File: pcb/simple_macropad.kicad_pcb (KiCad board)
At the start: 2 copper layers, 96 x 88 mm, 34 parts, among them J3 OLED_128x32, SW1 RotaryEncoder_Switch, SW2 RotaryEncoder_Switch, U2 PCF8574A, U3 MCU_Seeed_XIAO_RP2040

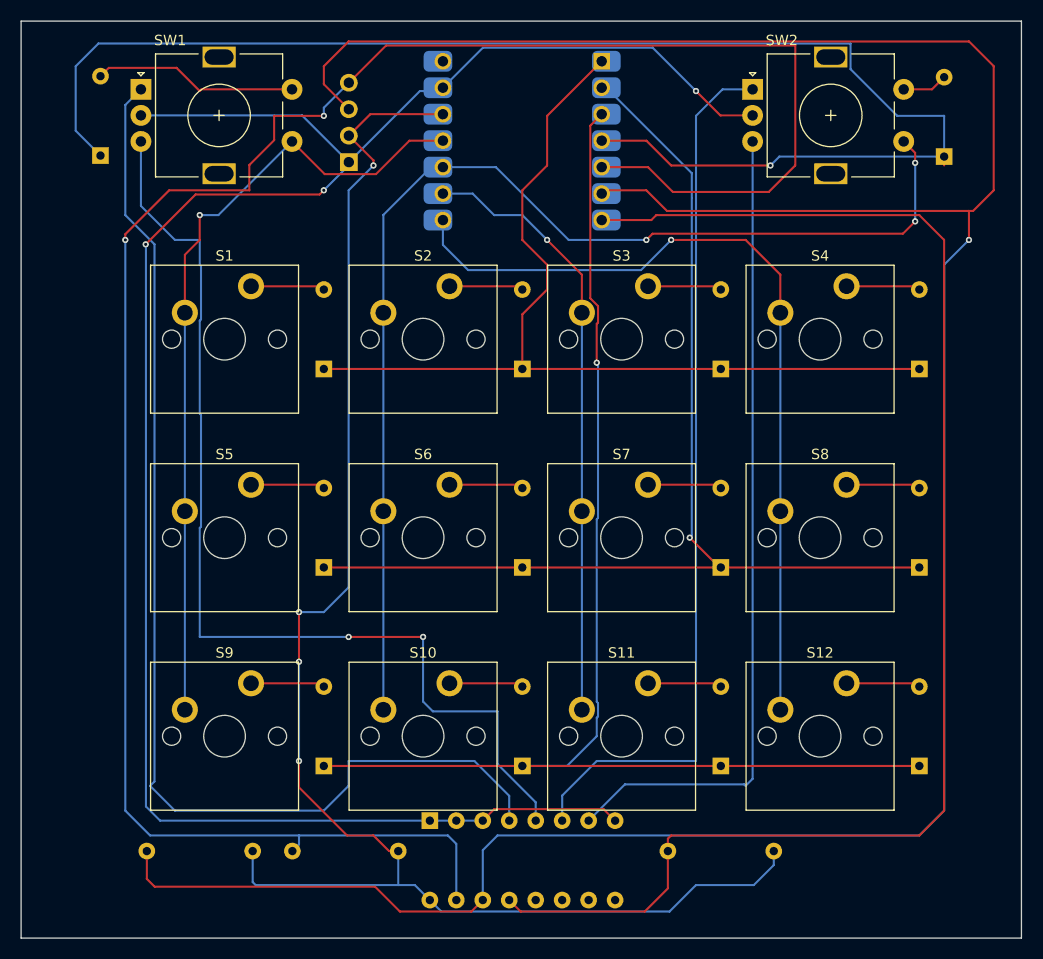
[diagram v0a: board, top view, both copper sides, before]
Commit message: updated pcb silkscreen
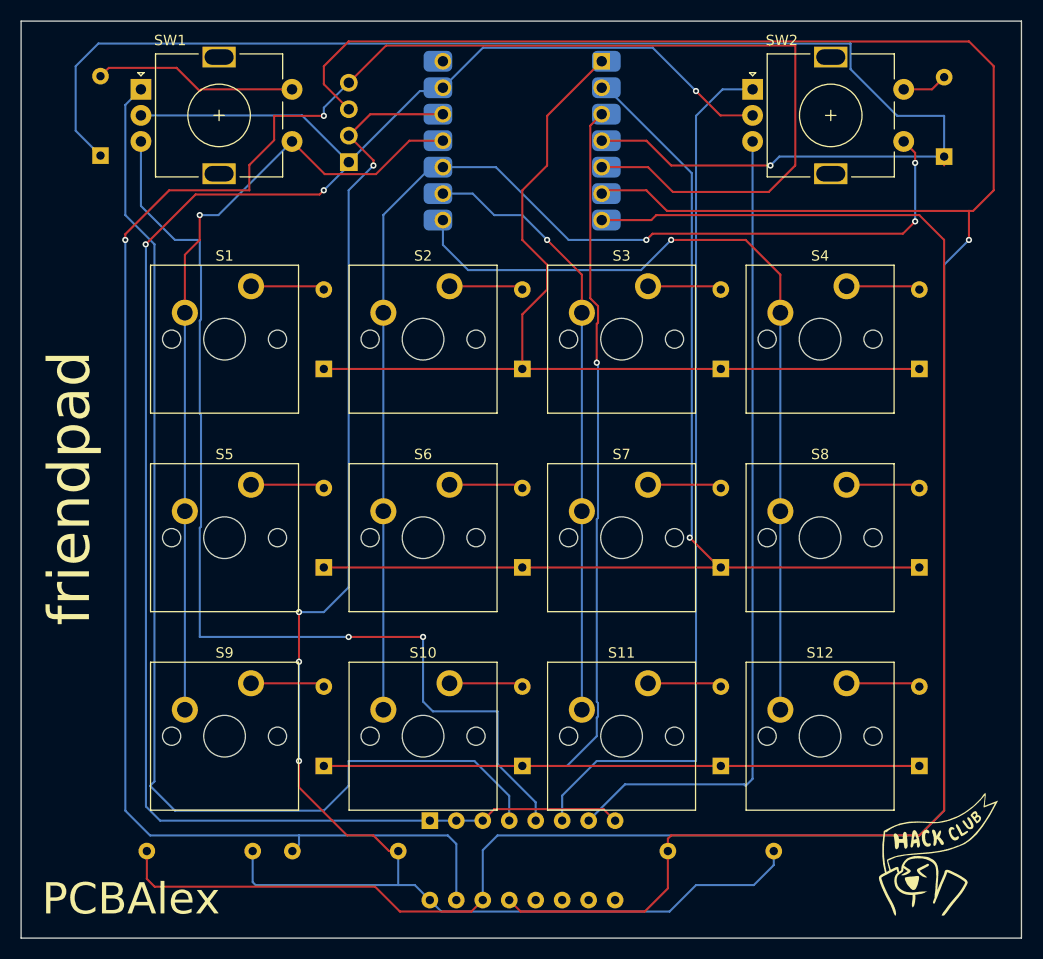
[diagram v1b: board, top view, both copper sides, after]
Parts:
- added  : LOGO, LOGO, F.Cu at (206.3, 106.6)
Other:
- board text added: "PCBAlex"
- board text added: "friendpad"
